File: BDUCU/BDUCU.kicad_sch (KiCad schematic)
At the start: 0 parts

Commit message: bducu updates
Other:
- added sheet SDC LATCH (SDCLATCH.kicad_sch)
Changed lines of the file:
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@@
 	(paper "A4")
 	(sheet
-		(at 121.666 116.84)
+		(at 130.048 115.824)
 		(size 34.544 28.194)
 		(exclude_from_sim no)
@@
 		)
 		(property "Sheetname" "Connectors"
-			(at 121.666 116.1284 0)
+			(at 130.048 115.1124 0)
 			(effects
 				(font
@@
 		)
 		(property "Sheetfile" "connectors.kicad_sch"
-			(at 121.666 145.6186 0)
+			(at 130.048 144.6026 0)
 			(effects
 				(font
@@
 				)
 			)
+		)
+	)
+	(sheet
+		(at 189.484 52.832)
+		(size 27.686 21.336)
+		(exclude_from_sim no)
+		(in_bom yes)
+		(on_board yes)
+		(dnp no)
+		(fields_autoplaced yes)
+		(stroke
+			(width 0.1524)
+			(type solid)
+		)
+		(fill
+			(color 0 0 0 0.0000)
+		)
+		(property "Sheetname" "SDC LATCH"
+			(at 189.484 52.1204 0)
+			(effects
+				(font
+					(size 1.27 1.27)
+				)
+				(justify left bottom)
+			)
+		)
+		(property "Sheetfile" "SDCLATCH.kicad_sch"
+			(at 189.484 74.7526 0)
+			(effects
+				(font
+					(size 1.27 1.27)
+				)
+				(justify left top)
+			)
+		)
+		(instances
+			(project "BDUCU"
+				(path "/9942a424-e19d-4ffb-8473-f960b5c811cf"
+					(page "14")
+				)
+			)

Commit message: bducu scheme done, waiting for check
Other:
- removed sheet SDC LATCH
- added sheet voltage regulator (voltage regulator.kicad_sch)
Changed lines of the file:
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@@
-	)
-	(sheet
-		(at 189.484 52.832)
-		(size 27.686 21.336)
-		(exclude_from_sim no)
-		(in_bom yes)
-		(on_board yes)
-		(dnp no)
-		(fields_autoplaced yes)
-		(stroke
-			(width 0.1524)
-			(type solid)
-		)
-		(fill
-			(color 0 0 0 0.0000)
-		)
-		(property "Sheetname" "SDC LATCH"
-			(at 189.484 52.1204 0)
-			(effects
-				(font
-					(size 1.27 1.27)
-				)
-				(justify left bottom)
-			)
-		)
-		(property "Sheetfile" "SDCLATCH.kicad_sch"
-			(at 189.484 74.7526 0)
-			(effects
-				(font
-					(size 1.27 1.27)
-				)
-				(justify left top)
-			)
-		)
-		(instances
-			(project "BDUCU"
-				(path "/9942a424-e19d-4ffb-8473-f960b5c811cf"
-					(page "14")
-				)
-			)
-		)
 	)
 	(sheet
@@
 	)
 	(sheet
-		(at 206.248 134.366)
+		(at 187.96 53.34)
+		(size 27.94 22.86)
+		(exclude_from_sim no)
+		(in_bom yes)
+		(on_board yes)
+		(dnp no)
+		(fields_autoplaced yes)
+		(stroke
+			(width 0.1524)
+			(type solid)
+		)
+		(fill
+			(color 0 0 0 0.0000)
+		)
+		(property "Sheetname" "voltage regulator"
+			(at 187.96 52.6284 0)
+			(effects
+				(font
+					(size 1.27 1.27)
+				)
+				(justify left bottom)
+			)
+		)
+		(property "Sheetfile" "voltage regulator.kicad_sch"
+			(at 187.96 76.7846 0)
+			(effects
+				(font
+					(size 1.27 1.27)
+				)
+				(justify left top)
+			)
+		)
+		(instances
+			(project "BDUCU"
+				(path "/9942a424-e19d-4ffb-8473-f960b5c811cf"
+					(page "15")
+				)
+			)
+		)
+	)
+	(sheet
+		(at 187.198 116.586)
 		(size 25.654 15.748)
 		(exclude_from_sim no)
@@
 		)
 		(property "Sheetname" "12V_Output"
-			(at 206.248 133.6544 0)
+			(at 187.198 115.8744 0)
 			(effects
 				(font
@@
 		)
 		(property "Sheetfile" "12v_output.kicad_sch"
-			(at 206.248 150.6986 0)
+			(at 187.198 132.9186 0)
 			(effects
 				(font
@@
 		)
 		(property "Field2" ""
-			(at 206.248 134.366 0)
+			(at 187.198 116.586 0)
 			(effects
 				(font

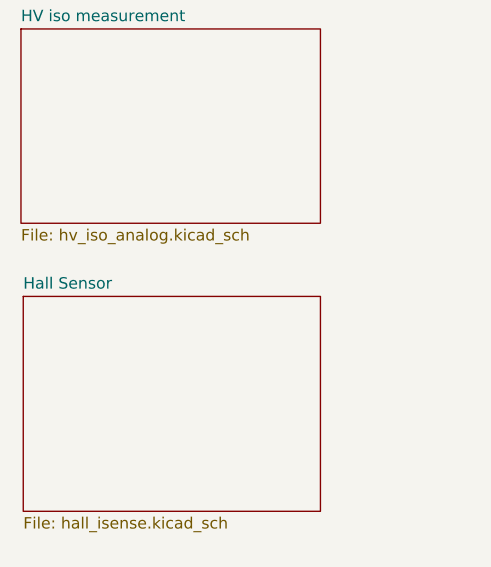
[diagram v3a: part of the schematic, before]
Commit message: bducu done I think added ntc
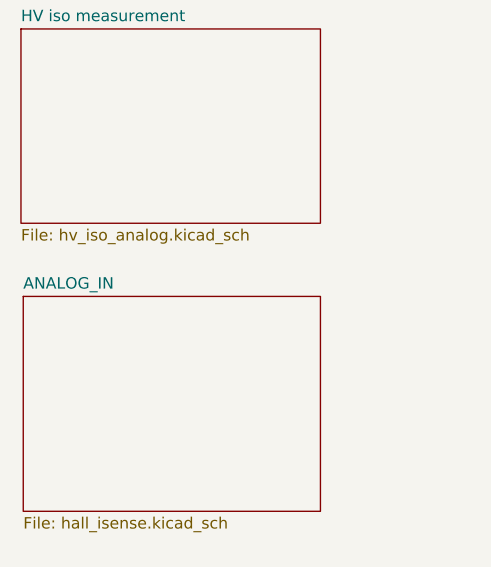
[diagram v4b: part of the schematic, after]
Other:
- sheet Hall Sensor renamed ANALOG_IN
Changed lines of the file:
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@@
 			(color 0 0 0 0.0000)
 		)
-		(property "Sheetname" "Hall Sensor"
+		(property "Sheetname" "ANALOG_IN"
 			(at 130.556 82.0924 0)
 			(effects
